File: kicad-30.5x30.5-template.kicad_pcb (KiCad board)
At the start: 2 copper layers, 37.5 x 37.5 mm, 4 parts

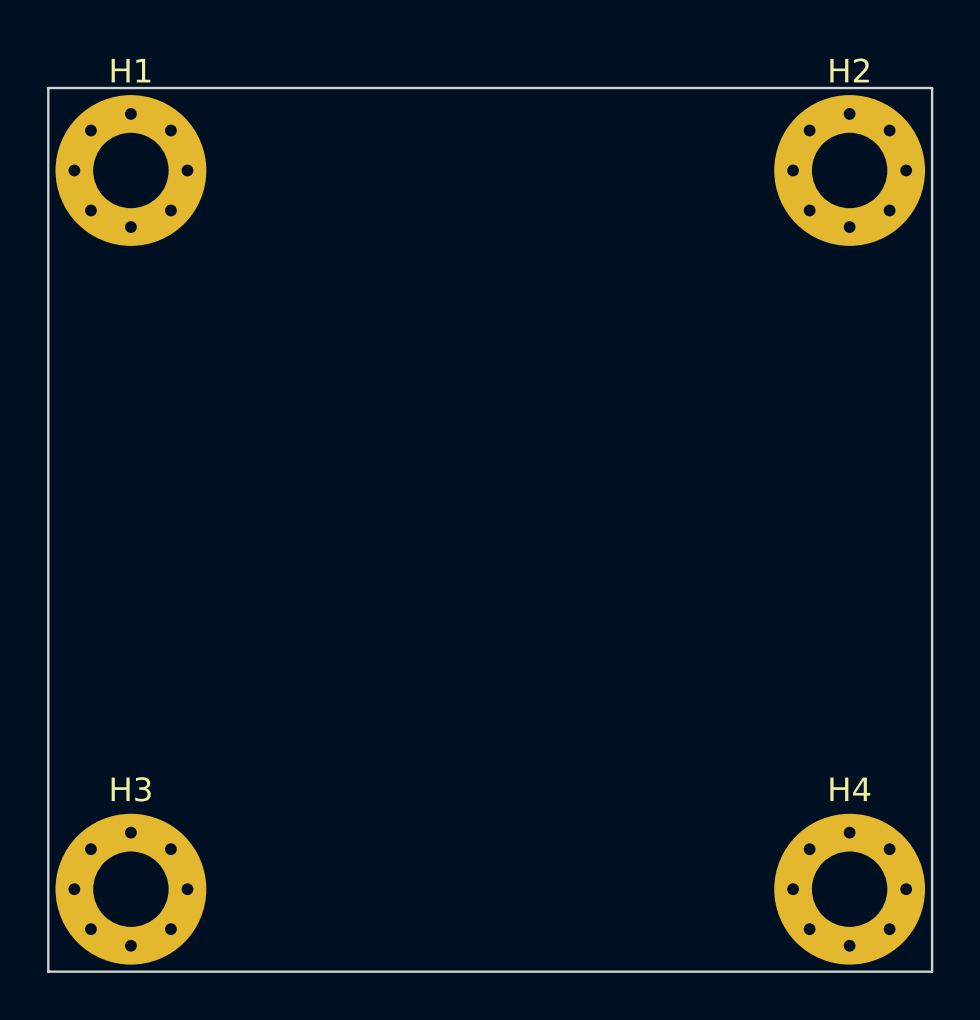
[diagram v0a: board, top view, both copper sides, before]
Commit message: Add a ground plane
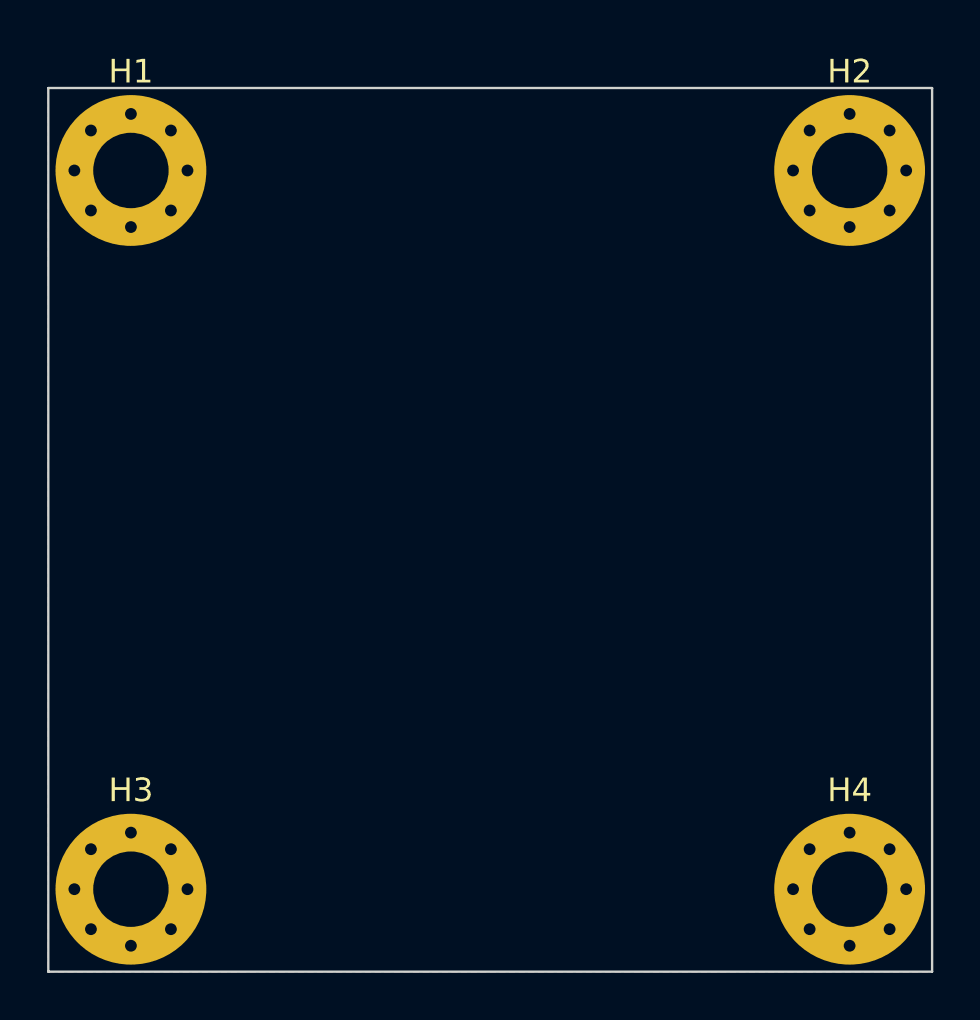
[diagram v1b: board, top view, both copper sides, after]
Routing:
- added copper zone on B.Cu, net GND
- added copper zone on F.Cu, net GND
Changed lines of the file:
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@@
 		(layer "Edge.Cuts")
 	)
+	(zone
+		(net 1)
+		(net_name "GND")
+		(layers "F&B.Cu")
+		(hatch edge 0.5)
+		(connect_pads
+			(clearance 0.5)
+		)
+		(min_thickness 0.25)
+		(filled_areas_thickness no)
+		(fill yes
+			(thermal_gap 0.5)
+			(thermal_bridge_width 0.5)
+		)
+		(polygon
+			(pts
+				(xy 136.3774 83.266) (xy 136.3774 120.7664) (xy 173.8836 120.7664) (xy 173.8836 83.266)
+			)
+		)
+	)
 )
